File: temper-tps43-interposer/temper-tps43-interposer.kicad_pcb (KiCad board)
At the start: 2 copper layers, 34 x 20 mm, 27 parts

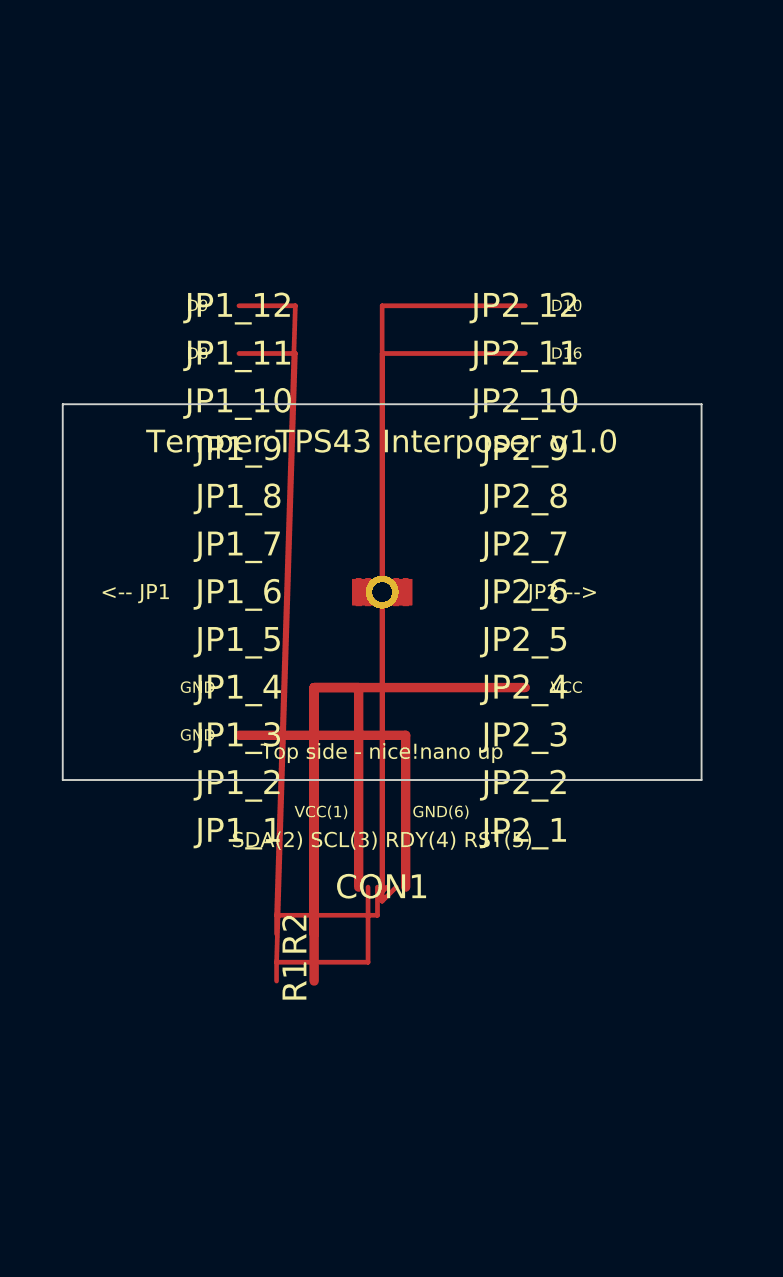
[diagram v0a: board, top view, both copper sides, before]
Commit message: Rewrite PCB from scratch with proper library footprint references
- Pin pads use Connector_PinHeader_2.54mm:PinHeader_1x01_P2.54mm_Vertical
- Resistors use Resistor_SMD:R_0805_2012Metric
- FFC connector uses our custom TPS43_FFC_06 footprint
- All properties include proper layer, uuid, and effects blocks
- Board outline 34x20mm, full layer set matching KiCAD 9 format
- Fixed missing (layers) wrapper causing unbalanced parens
- gen_pcb.py: reproducible generator, run to regenerate PCB
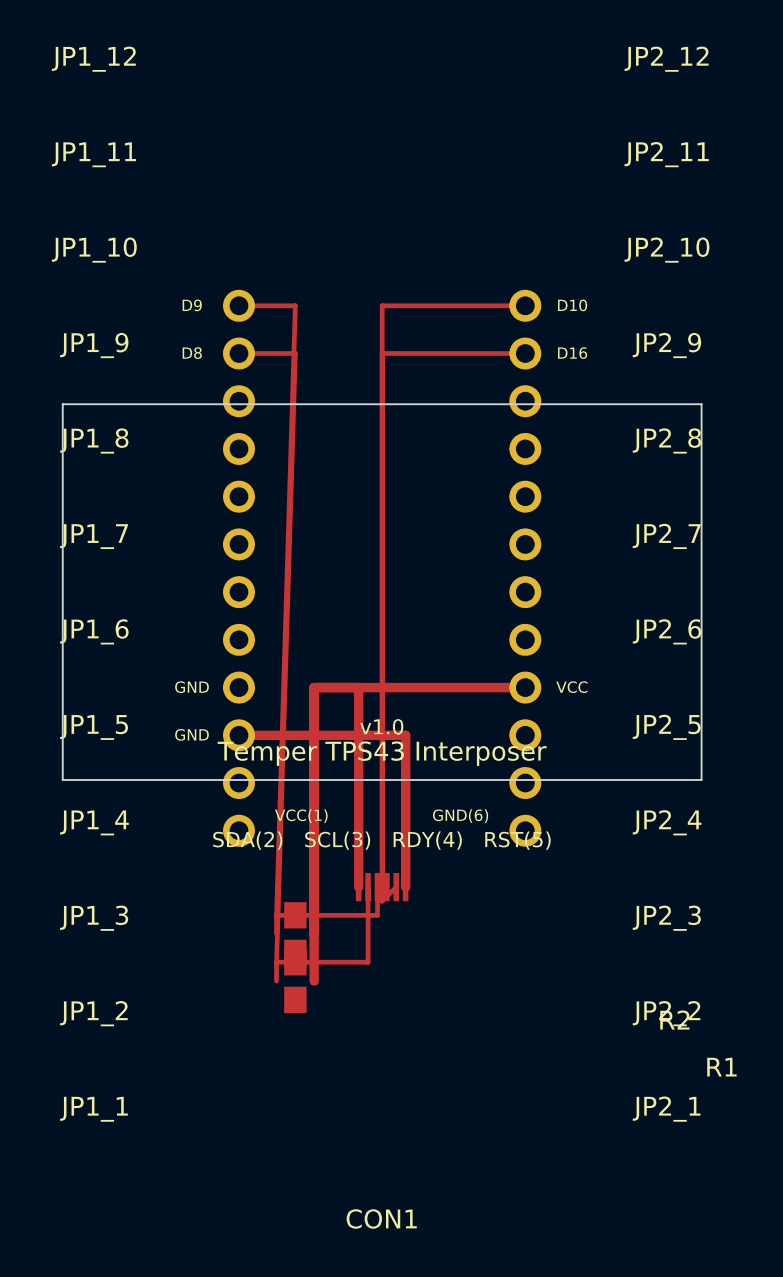
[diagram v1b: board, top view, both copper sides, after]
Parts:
- CON1: value (none) -> TPS43 FFC; footprint (none) -> temper-tps43-interposer:TPS43_FFC_06
- JP1_1: value (none) -> D1; footprint (none) -> Connector_PinHeader_2.54mm:PinHeader_1x01_P2.54mm_Vertical
- JP1_10: value (none) -> D7; footprint (none) -> Connector_PinHeader_2.54mm:PinHeader_1x01_P2.54mm_Vertical
- JP1_11: value (none) -> D8; footprint (none) -> Connector_PinHeader_2.54mm:PinHeader_1x01_P2.54mm_Vertical
- JP1_12: value (none) -> D9; footprint (none) -> Connector_PinHeader_2.54mm:PinHeader_1x01_P2.54mm_Vertical
- JP1_2: value (none) -> D0; footprint (none) -> Connector_PinHeader_2.54mm:PinHeader_1x01_P2.54mm_Vertical
- JP1_3, JP1_4, JP2_2: value (none) -> GND; footprint (none) -> Connector_PinHeader_2.54mm:PinHeader_1x01_P2.54mm_Vertical
- JP1_5: value (none) -> D2; footprint (none) -> Connector_PinHeader_2.54mm:PinHeader_1x01_P2.54mm_Vertical
- JP1_6: value (none) -> D3; footprint (none) -> Connector_PinHeader_2.54mm:PinHeader_1x01_P2.54mm_Vertical
- JP1_7: value (none) -> D4; footprint (none) -> Connector_PinHeader_2.54mm:PinHeader_1x01_P2.54mm_Vertical
- JP1_8: value (none) -> D5; footprint (none) -> Connector_PinHeader_2.54mm:PinHeader_1x01_P2.54mm_Vertical
- JP1_9: value (none) -> D6; footprint (none) -> Connector_PinHeader_2.54mm:PinHeader_1x01_P2.54mm_Vertical
- JP2_1: value (none) -> RAW; footprint (none) -> Connector_PinHeader_2.54mm:PinHeader_1x01_P2.54mm_Vertical
- JP2_10: value (none) -> D14; footprint (none) -> Connector_PinHeader_2.54mm:PinHeader_1x01_P2.54mm_Vertical
- JP2_11: value (none) -> D16; footprint (none) -> Connector_PinHeader_2.54mm:PinHeader_1x01_P2.54mm_Vertical
- JP2_12: value (none) -> D10; footprint (none) -> Connector_PinHeader_2.54mm:PinHeader_1x01_P2.54mm_Vertical
- JP2_3: value (none) -> RST; footprint (none) -> Connector_PinHeader_2.54mm:PinHeader_1x01_P2.54mm_Vertical
- JP2_4: value (none) -> VCC; footprint (none) -> Connector_PinHeader_2.54mm:PinHeader_1x01_P2.54mm_Vertical
- JP2_5: value (none) -> D21; footprint (none) -> Connector_PinHeader_2.54mm:PinHeader_1x01_P2.54mm_Vertical
- JP2_6: value (none) -> D20; footprint (none) -> Connector_PinHeader_2.54mm:PinHeader_1x01_P2.54mm_Vertical
- JP2_7: value (none) -> D19; footprint (none) -> Connector_PinHeader_2.54mm:PinHeader_1x01_P2.54mm_Vertical
- JP2_8: value (none) -> D18; footprint (none) -> Connector_PinHeader_2.54mm:PinHeader_1x01_P2.54mm_Vertical
- JP2_9: value (none) -> D15; footprint (none) -> Connector_PinHeader_2.54mm:PinHeader_1x01_P2.54mm_Vertical
- R1, R2: value (none) -> 2.2k; footprint (none) -> Resistor_SMD:R_0805_2012Metric
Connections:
- CON1 pad 1: (no net) -> VCC
- CON1 pad 2: (no net) -> SDA
- CON1 pad 3: (no net) -> SCL
- CON1 pad 4: (no net) -> RDY
- CON1 pad 5: (no net) -> RST
- CON1 pad 6: (no net) -> GND
- JP1_11 pad 1: (no net) -> SDA
- JP1_12 pad 1: (no net) -> SCL
- JP1_3 pad 1: (no net) -> GND
- JP1_4 pad 1: (no net) -> GND
- JP2_11 pad 1: (no net) -> RST
- JP2_12 pad 1: (no net) -> RDY
- JP2_2 pad 1: (no net) -> GND
- JP2_4 pad 1: (no net) -> VCC
- R1 pad 1: (no net) -> SDA
- R1 pad 2: (no net) -> VCC
- R2 pad 1: (no net) -> SCL
- R2 pad 2: (no net) -> VCC
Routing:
- net 0: track 235.5 -> 0.00 mm
- net VCC: track 0.00 -> 53.0 mm
- net SDA: track 0.00 -> 45.3 mm
- net SCL: track 0.00 -> 43.3 mm
- net RDY: track 0.00 -> 39.2 mm
- net RST: track 0.00 -> 37.8 mm
- net GND: track 0.00 -> 16.9 mm
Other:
- board text added: "Temper TPS43 Interposer"
- board text added: "v1.0"
- board text removed: "<-- JP1"
- board text removed: "JP2 -->"
- board text removed: "Temper TPS43 Interposer v1.0"
- board text removed: "Top side - nice!nano up"
